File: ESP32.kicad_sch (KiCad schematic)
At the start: 30 parts, among them J201 GPIO, J202 Power, J203 Conn_01x01, J206 IO, J207 Conn_01x07, U201 ESP32-WROOM-32E

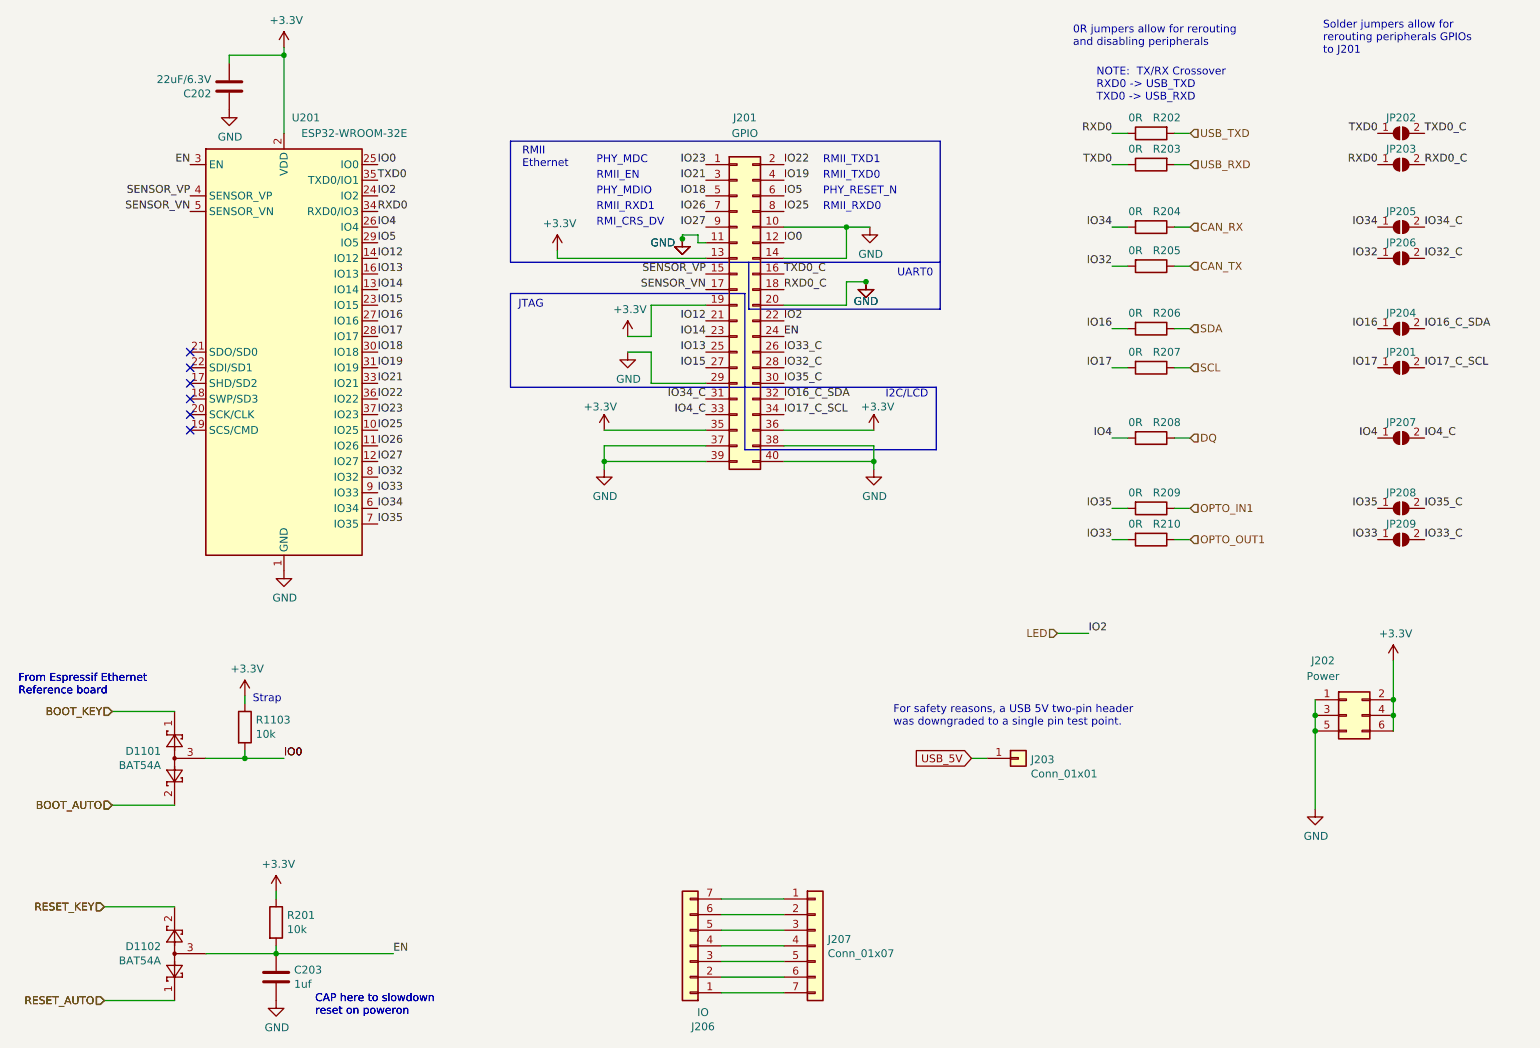
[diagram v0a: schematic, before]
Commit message: Go back to ISO1050 for CAN transceiver
Also add CAN RX and TX LEDs and beef up buck capacitors
as much as space allows.
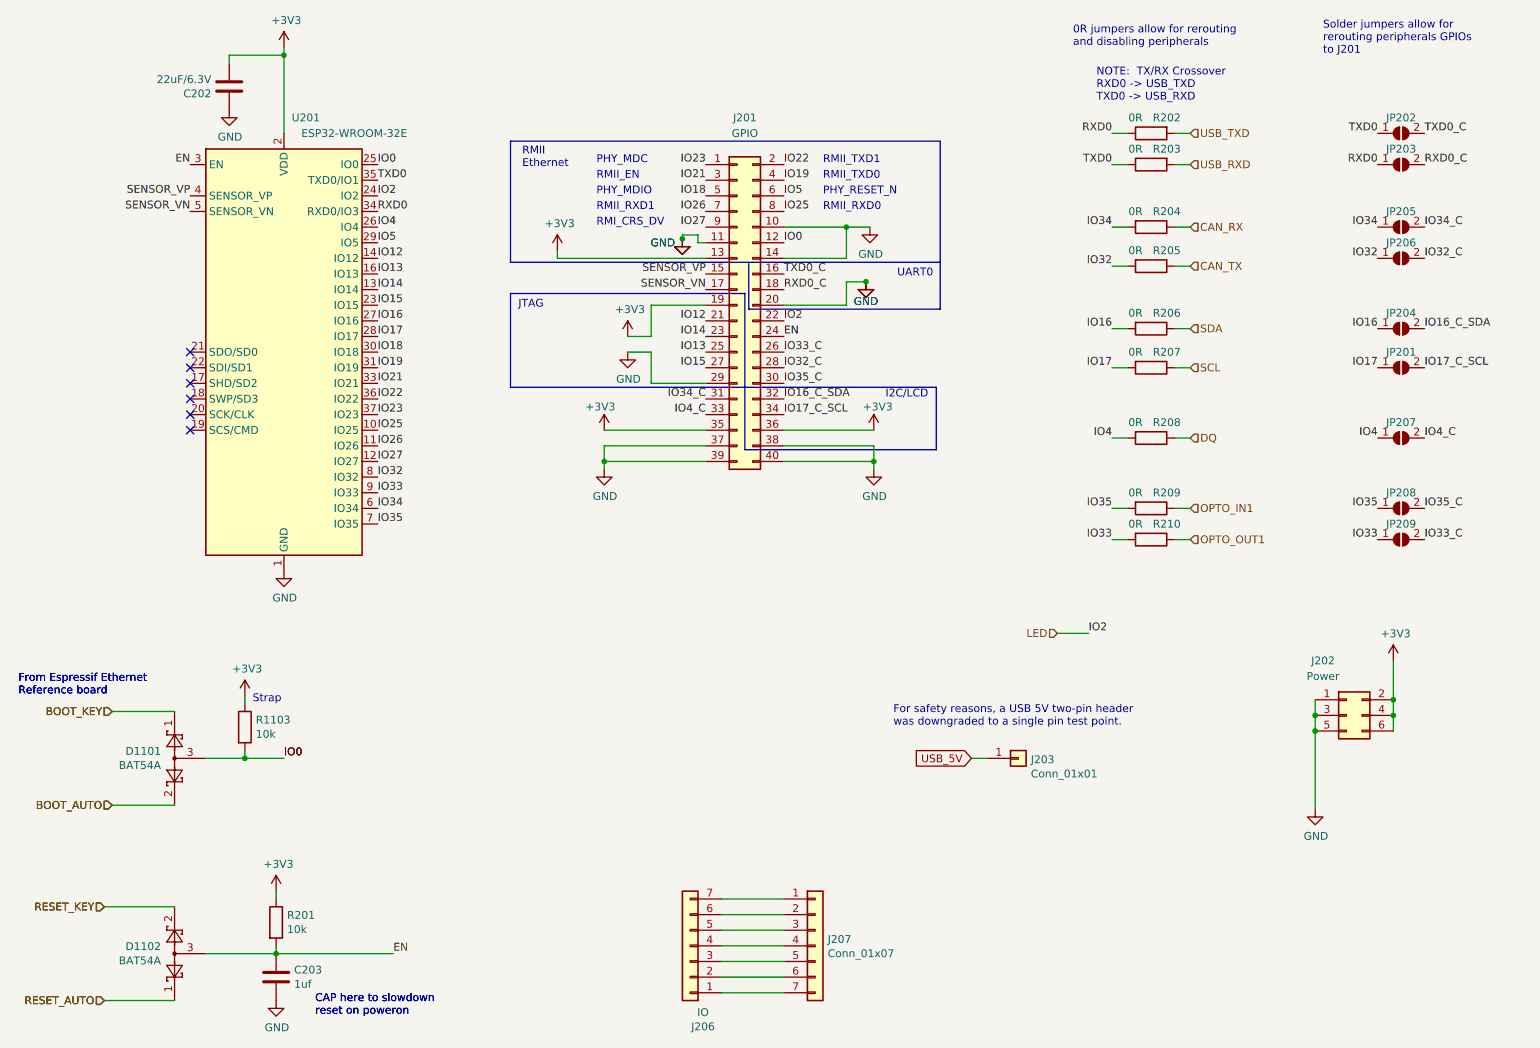
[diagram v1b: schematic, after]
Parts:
- D1101, D1102: LCSC C134404 -> C78261
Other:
- company: Hat Labs Ltd -> Hat Labs Oy
- title: Sailor Hat with ESP32 -> SH-ESP32

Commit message: Change buck converter to LMR54410
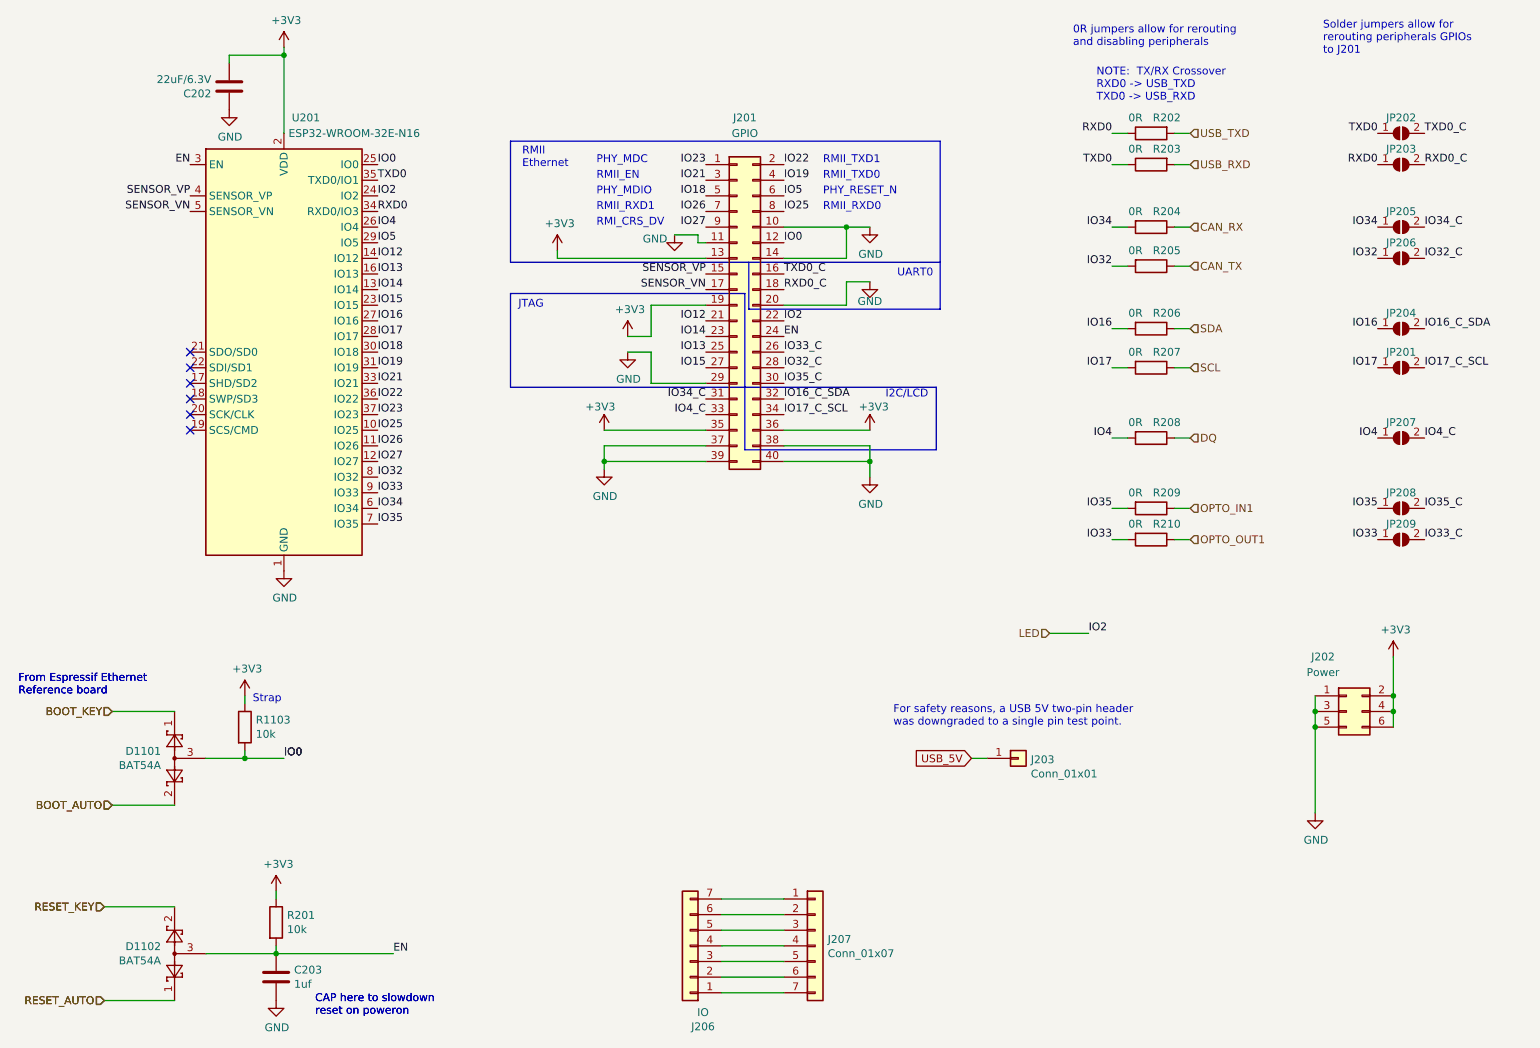
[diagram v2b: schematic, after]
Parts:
- U201: value ESP32-WROOM-32E -> ESP32-WROOM-32E-N16; footprint SH-ESP32:ESP32-WROOM-32-HandSolder -> SH-ESP32:ESP32-WROOM-32D; LCSC C701341 -> C701343
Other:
- moved on the sheet: J202
